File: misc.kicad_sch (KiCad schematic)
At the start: 22 parts, among them J4 PinSocket_2x11_P2.54mm_Drill1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, U2 NTS0102_TSSOP, U3 NTS0102_TSSOP, Y1 Oscillator_25MHz_511ABA25M000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, Y2 Resonator_50MHz_XRCGE

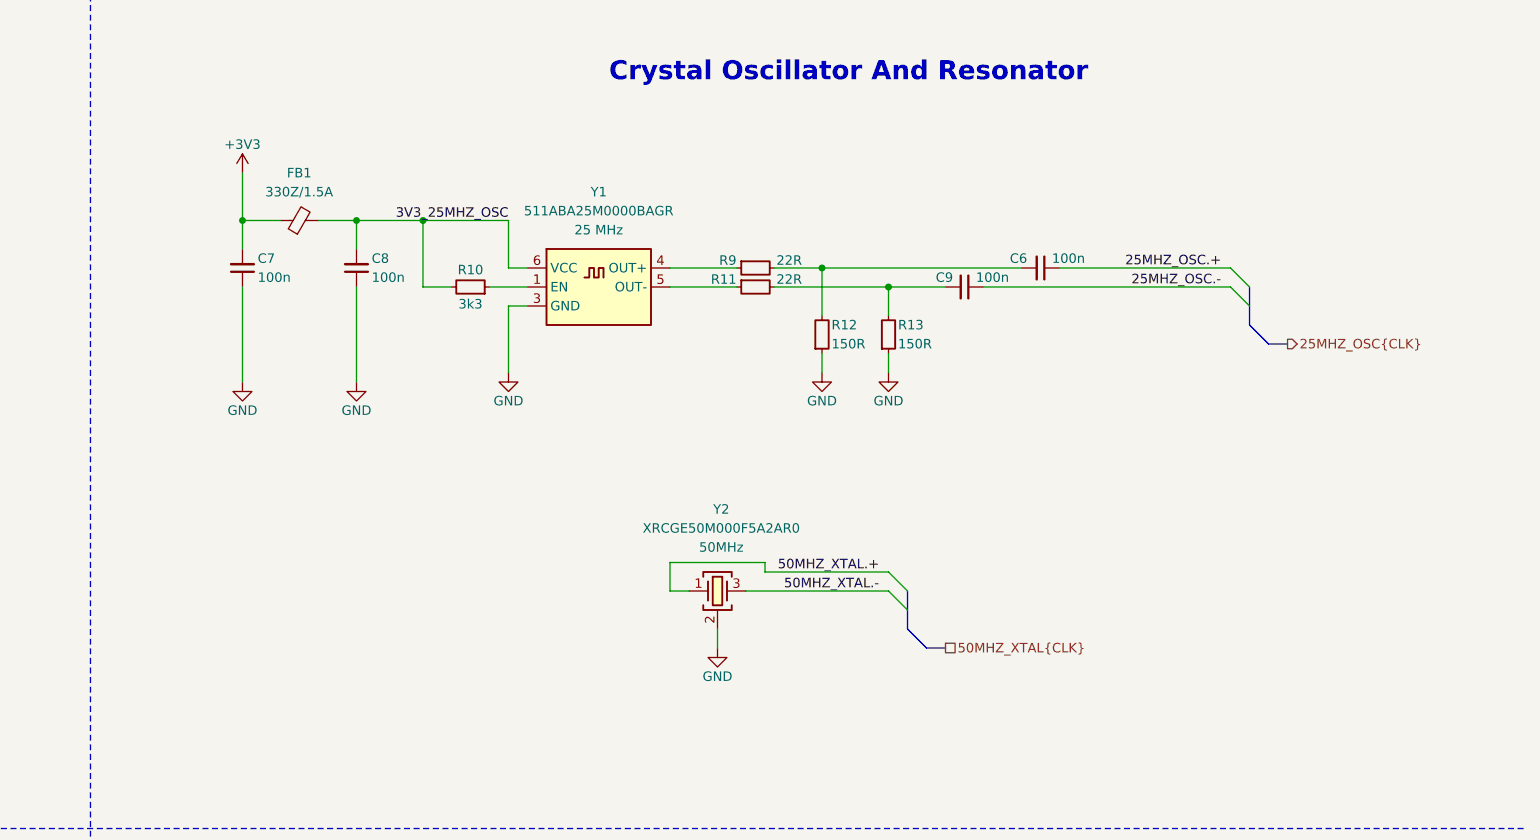
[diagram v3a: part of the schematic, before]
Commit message: [#80813] WIP: Adjust passives values, add missing load capacitors for the 50MHz resonator
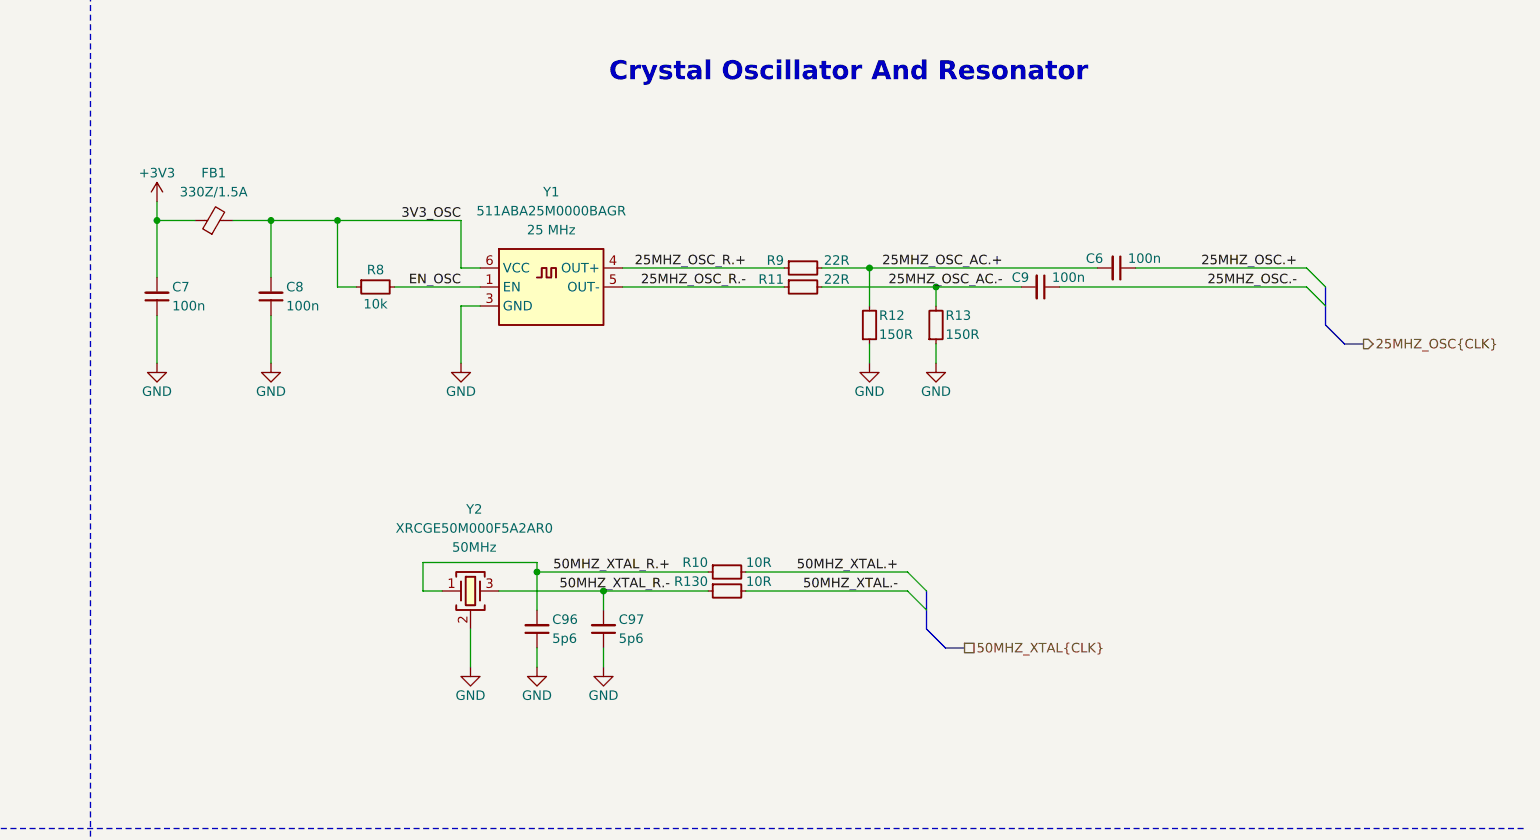
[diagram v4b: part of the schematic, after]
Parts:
- removed R10: R_3k3_0402, antmicro-footprints:R_0402_1005Metric, symbol antmicroResistors0402:R_3k3_0402
- added C96, C97: C_5p6_0402, antmicro-footprints:C_0402_1005Metric, symbol antmicroCapacitors0402:C_5p6_0402
- added R10, R130: R_10R_0402, antmicro-footprints:R_0402_1005Metric, symbol antmicroResistors0402:R_10R_0402
- added R8: R_10k_0402, antmicro-footprints:R_0402_1005Metric, symbol antmicroResistors0402:R_10k_0402
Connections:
- net 50MHZ_XTAL.+: now also R10.2; no longer Y2.1
- net 50MHZ_XTAL.-: now also R130.2; no longer Y2.3
- net GND: now also C96.1, C97.1
- net 25MHZ_OSC_AC.-: now reaches C9.2, R11.2, R13.2
- net 25MHZ_OSC_AC.+: now reaches C6.2, R12.2, R9.2
- net 25MHZ_OSC_R.+: now reaches R9.1, Y1.4 (OUT+)
- net EN_OSC: now reaches Y1.1 (EN)
- net EN_OSC: now also R8.2
- net 25MHZ_OSC_R.-: now reaches R11.1, Y1.5 (OUT-)
- net 3V3_25MHZ_OSC renamed 3V3_OSC
- net 3V3_OSC: now also R8.1
- new net 50MHZ_XTAL_R.+: C96.2, R10.1, Y2.1
- new net 50MHZ_XTAL_R.-: C97.2, R130.1, Y2.3
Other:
- moved on the sheet: C6, C7, C8, C9, FB1, R11, R12, R13, R9, Y1, Y2

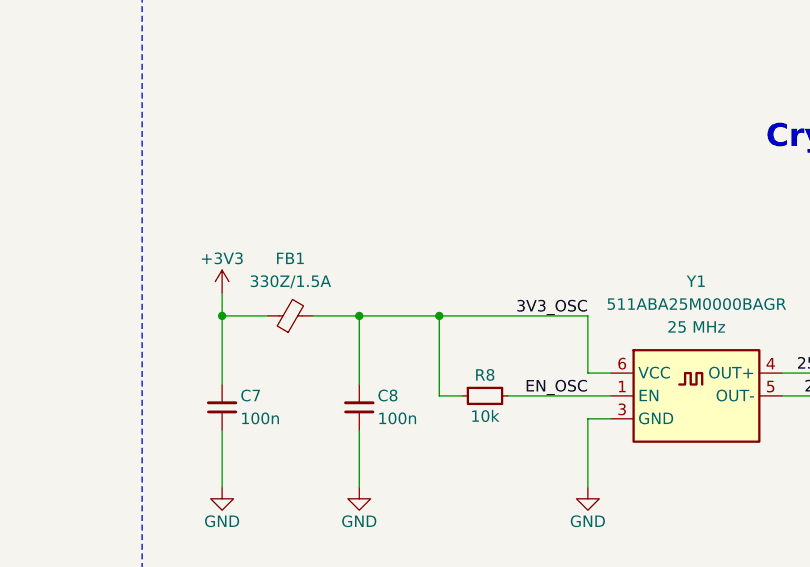
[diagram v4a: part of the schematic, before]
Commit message: [#80813] Adjust passives values, add remaining decoupling capacitors
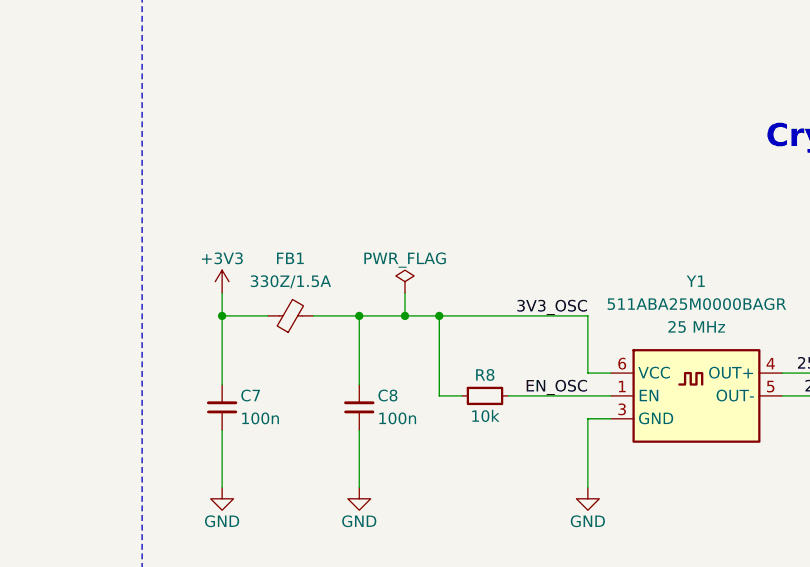
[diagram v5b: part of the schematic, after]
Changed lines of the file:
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@@
 	)
 	(junction
+		(at 245.11 62.23)
+		(diameter 0)
+		(color 0 0 0 0)
+	)
+	(junction
 		(at 331.47 214.63)
 		(diameter 0)
@@
 	(wire
 		(pts
+			(xy 245.11 59.69) (xy 245.11 62.23)
+		)
+		(stroke
+			(width 0)
+			(type default)
+		)
+	)
+	(wire
+		(pts
 			(xy 248.92 62.23) (xy 248.92 71.12)
 		)
@@
 	(wire
 		(pts
-			(xy 240.03 62.23) (xy 248.92 62.23)
+			(xy 240.03 62.23) (xy 245.11 62.23)
 		)
 		(stroke
@@
 	(wire
 		(pts
+			(xy 245.11 62.23) (xy 248.92 62.23)
+		)
+		(stroke
+			(width 0)
+			(type default)
+		)
+	)
+	(wire
+		(pts
 			(xy 105.41 194.31) (xy 123.19 194.31)
 		)
@@
 					(unit 1)
 				)
+			)
+		)
+	)
+	(symbol
+		(lib_id "antmicropower:PWR_FLAG")
+		(at 245.11 59.69 0)
+		(unit 1)
+		(exclude_from_sim no)
+		(in_bom yes)
+		(on_board yes)
+		(dnp no)
+		(property "Reference" "#FLG02"
+			(at 245.11 57.785 0)
+			(effects
+				(font
+					(size 1.27 1.27)
+				)
+				(hide yes)
+			)
+		)
+		(property "Value" "PWR_FLAG"
+			(at 245.11 55.88 0)
+			(effects
+				(font
+					(size 1.27 1.27)
+				)
+			)
+		)
+		(property "Footprint" ""
+			(at 245.11 59.69 0)
+			(effects
+				(font
+					(size 1.27 1.27)
+				)
+				(hide yes)
+			)
+		)
+		(property "Datasheet" ""
+			(at 245.11 59.69 0)
+			(effects
+				(font
+					(size 1.27 1.27)
+				)
+				(hide yes)
+			)
+		)
+		(property "Description" ""
+			(at 245.11 59.69 0)
+			(effects
+				(font
+					(size 1.27 1.27)
+				)
+				(hide yes)
+			)
+		)
+		(pin "1"
+		)
+		(instances
+			(project ""
+				(path "/04bda987-e5eb-48b4-9e90-d8211dc11b39/d68fe835-a207-4e7d-ae52-7b00c0459c21"
+					(reference "#FLG02")
+					(unit 1)
+				)

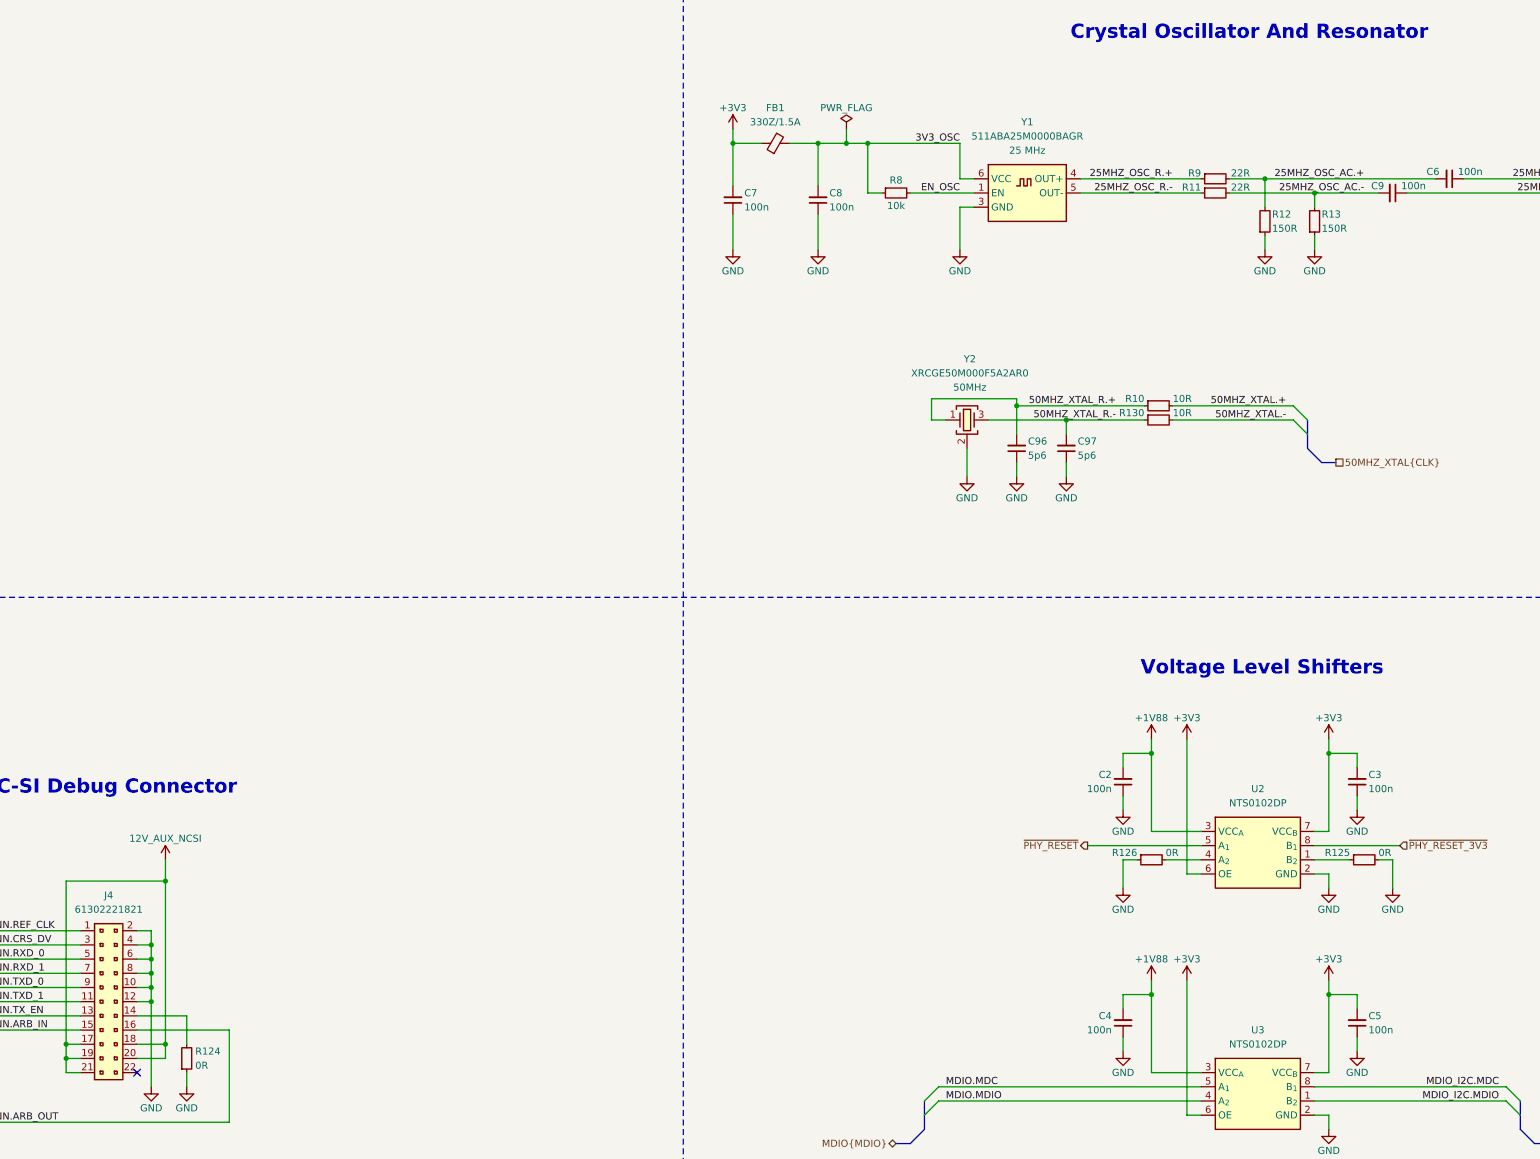
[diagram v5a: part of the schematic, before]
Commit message: [#80813] Add OCuLink connector
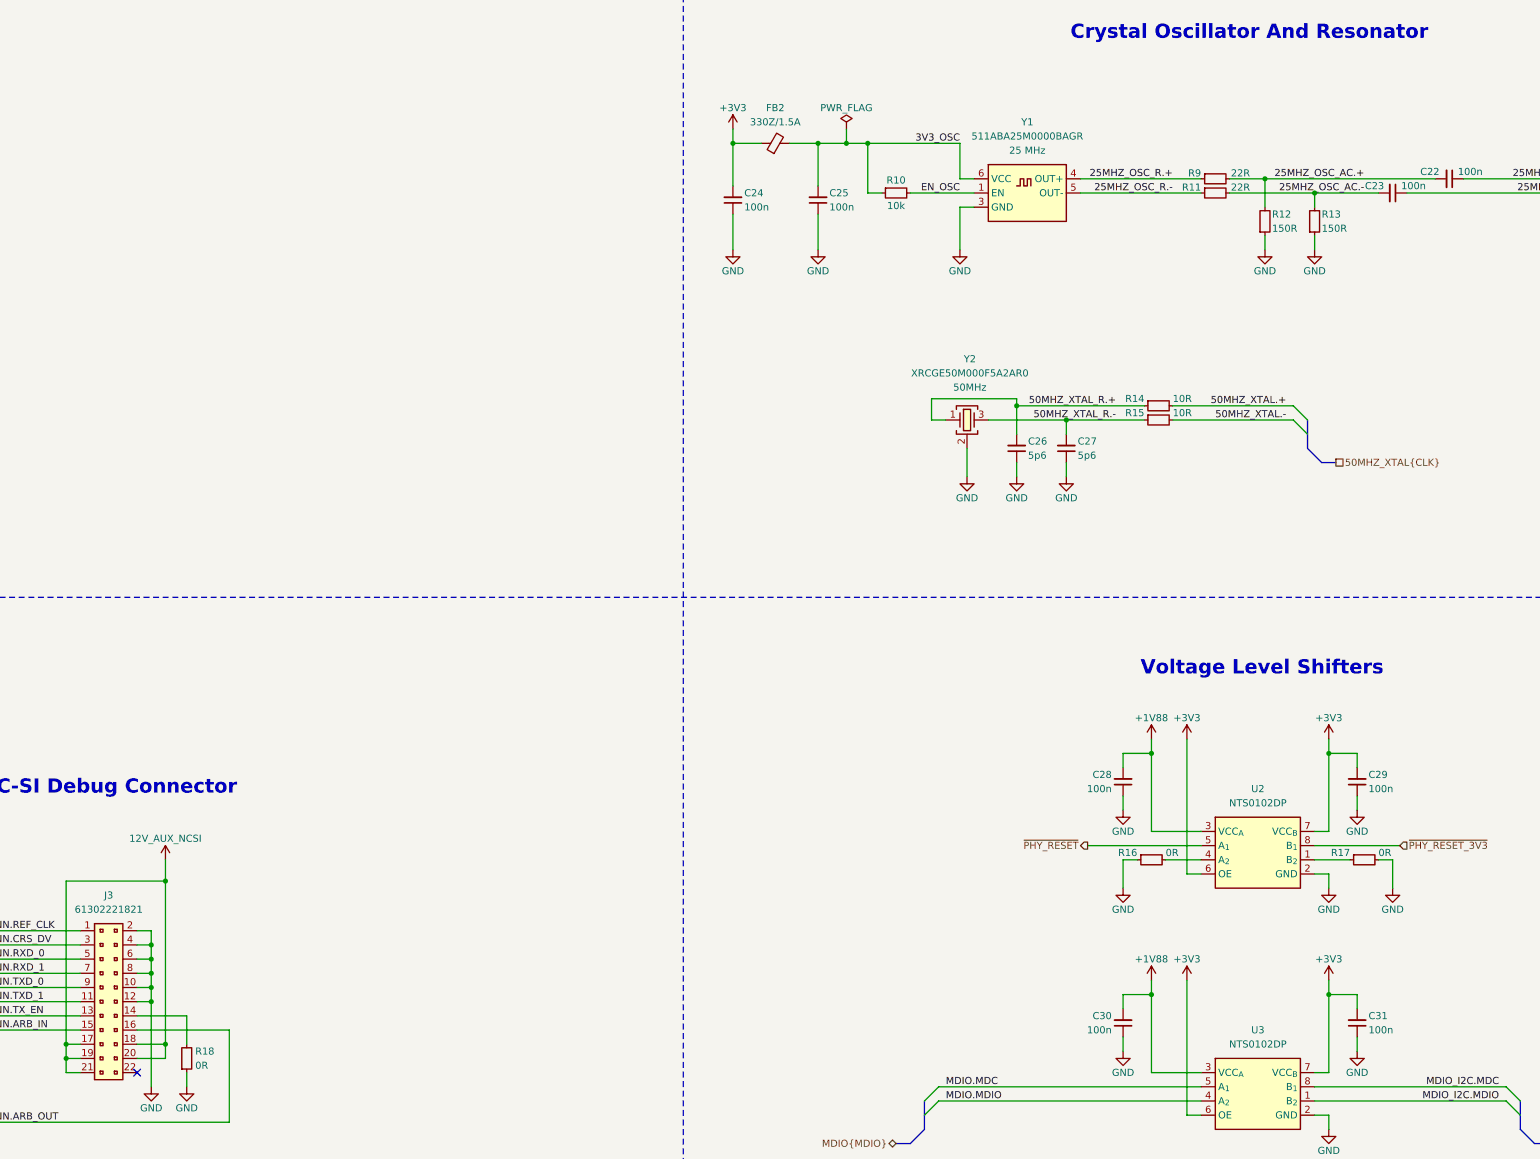
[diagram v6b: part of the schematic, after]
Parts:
- renumbered C6 to C22, C9 to C23, C7 to C24, C8 to C25, C96 to C26, C97 to C27, C2 to C28, C3 to C29, C4 to C30, C5 to C31, FB1 to FB2, J4 to J3, R8 to R10, R10 to R14, R130 to R15, R126 to R16, R125 to R17, R124 to R18

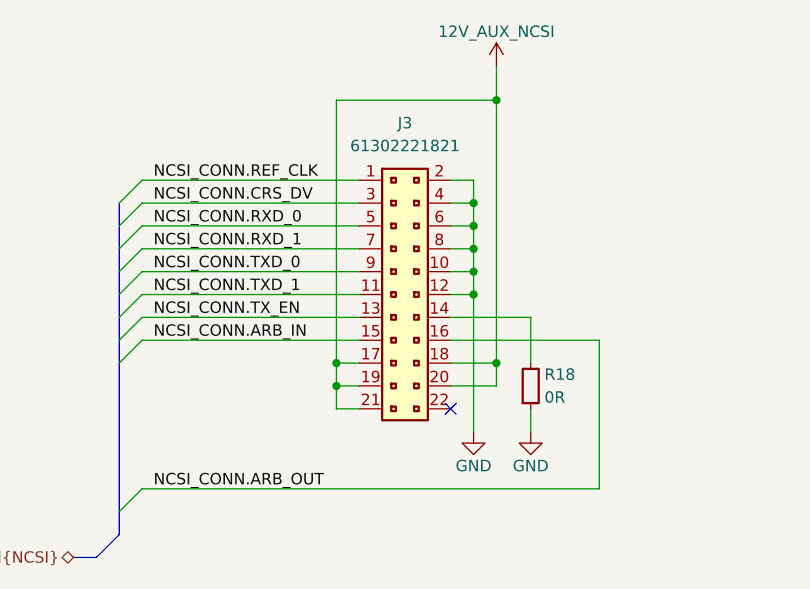
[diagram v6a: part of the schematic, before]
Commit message: [#80813] Add power input connectors, heatsink, mounting, draft component placement
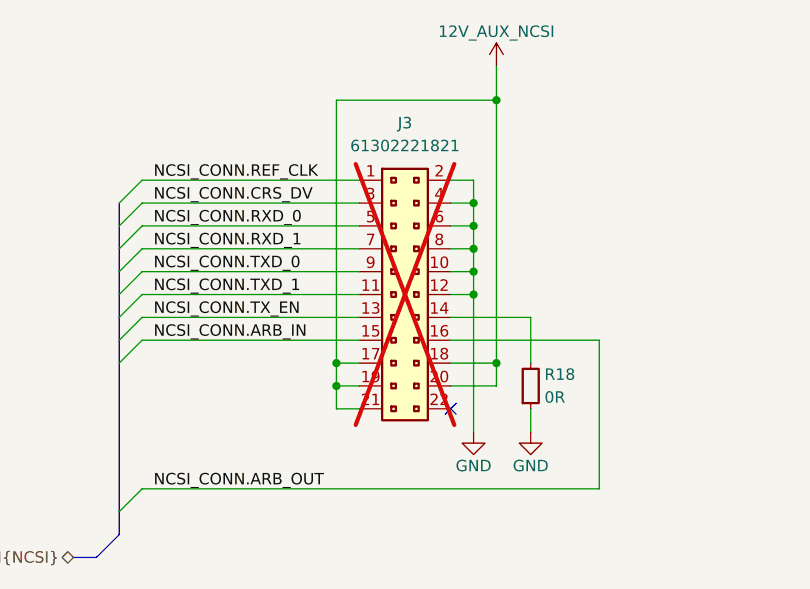
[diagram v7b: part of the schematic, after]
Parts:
- J3: now not fitted; now left out of the parts list
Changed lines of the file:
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@@
 		(unit 1)
 		(exclude_from_sim no)
-		(in_bom yes)
+		(in_bom no)
 		(on_board yes)
-		(dnp no)
+		(dnp yes)
 		(fields_autoplaced yes)
 		(property "Reference" "J3"
